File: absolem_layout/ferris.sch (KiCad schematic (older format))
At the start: 103 parts, among them IC1 NUF2221W1T2G, J1 USB C, K0_0 KEYSW, K0_1 KEYSW, K0_2 KEYSW, K0_3 KEYSW, K0_4 KEYSW, K0_5 KEYSW, K0_6 KEYSW, K0_7 KEYSW, K0_8 KEYSW, K0_9 KEYSW, K1_0 KEYSW, K1_1 KEYSW, K1_2 KEYSW, K1_3 KEYSW, K1_4 KEYSW, K1_5 KEYSW, K1_6 KEYSW, K1_7 KEYSW, K1_8 KEYSW, K1_9 KEYSW, K2_0 KEYSW, K2_1 KEYSW, K2_2 KEYSW, K2_3 KEYSW, K2_4 KEYSW, K2_5 KEYSW, K2_6 KEYSW, K2_7 KEYSW, K2_8 KEYSW, K2_9 KEYSW, K3_2 KEYSW, K3_3 KEYSW, K3_4 KEYSW, K3_5 KEYSW, K3_6 KEYSW, K3_7 KEYSW, SW1 SW_PUSH, SW2 SW_PUSH, U1 ATmega32U4-AU, U2 TLV70012_SOT23-5, U3 STM32F303CBTx, Y1 Crystal, Y2 8MHz

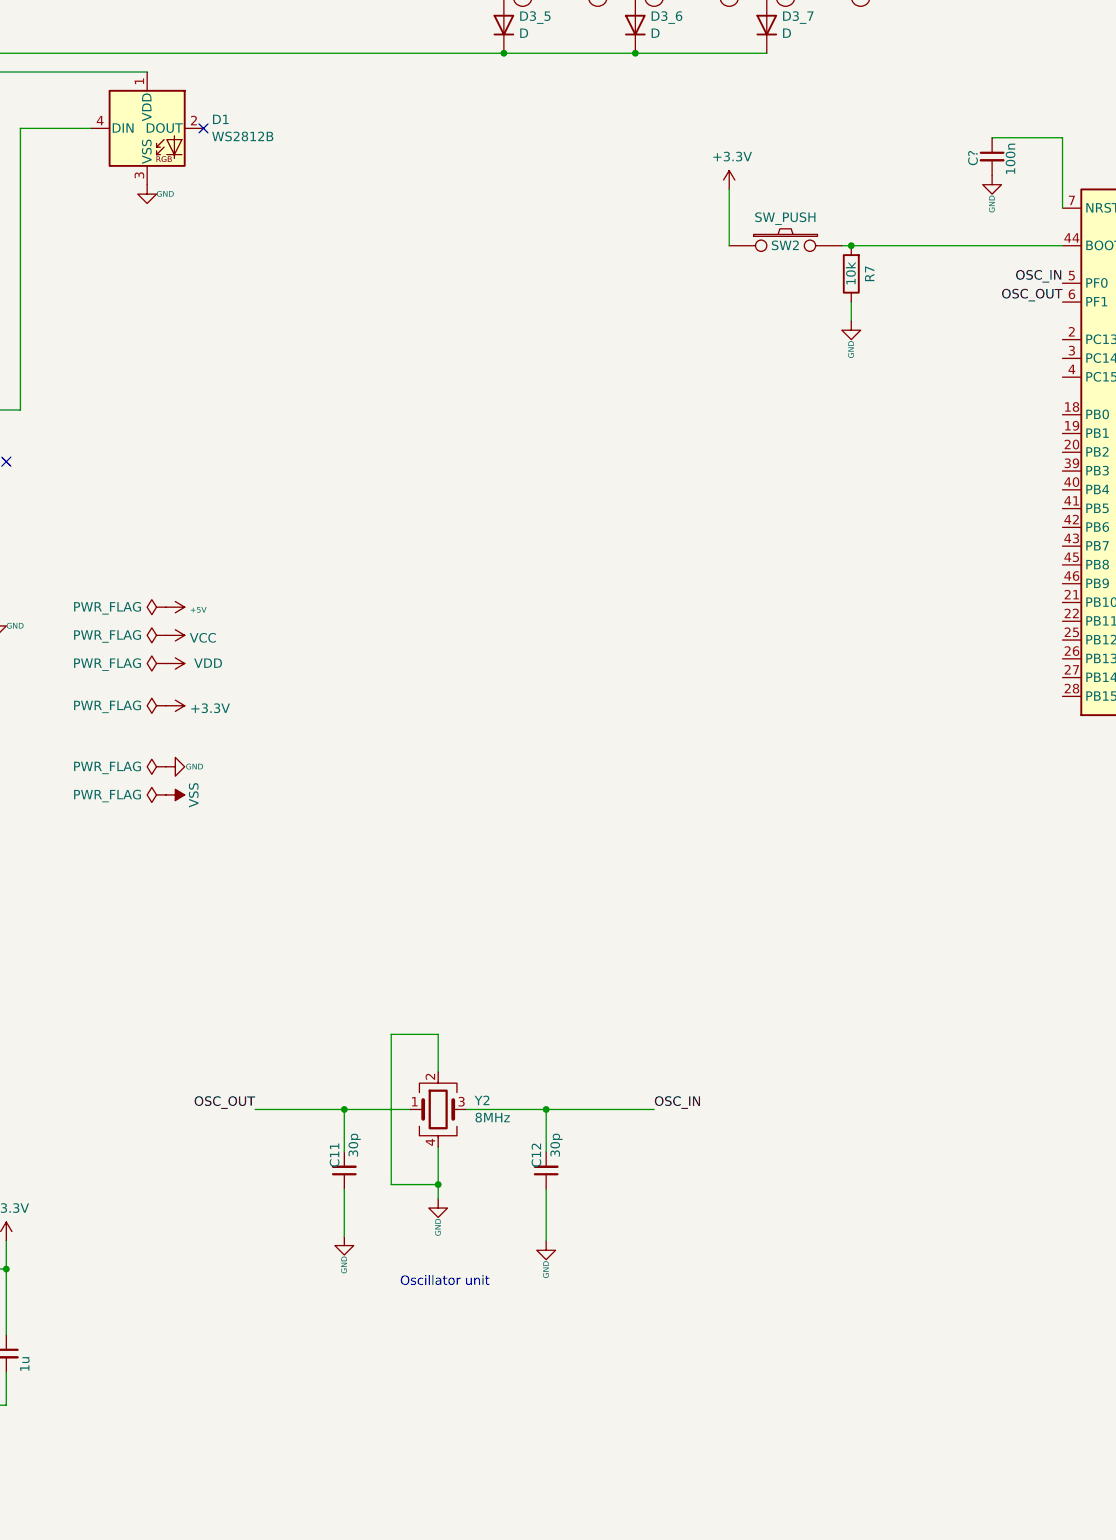
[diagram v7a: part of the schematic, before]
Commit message: More labelling
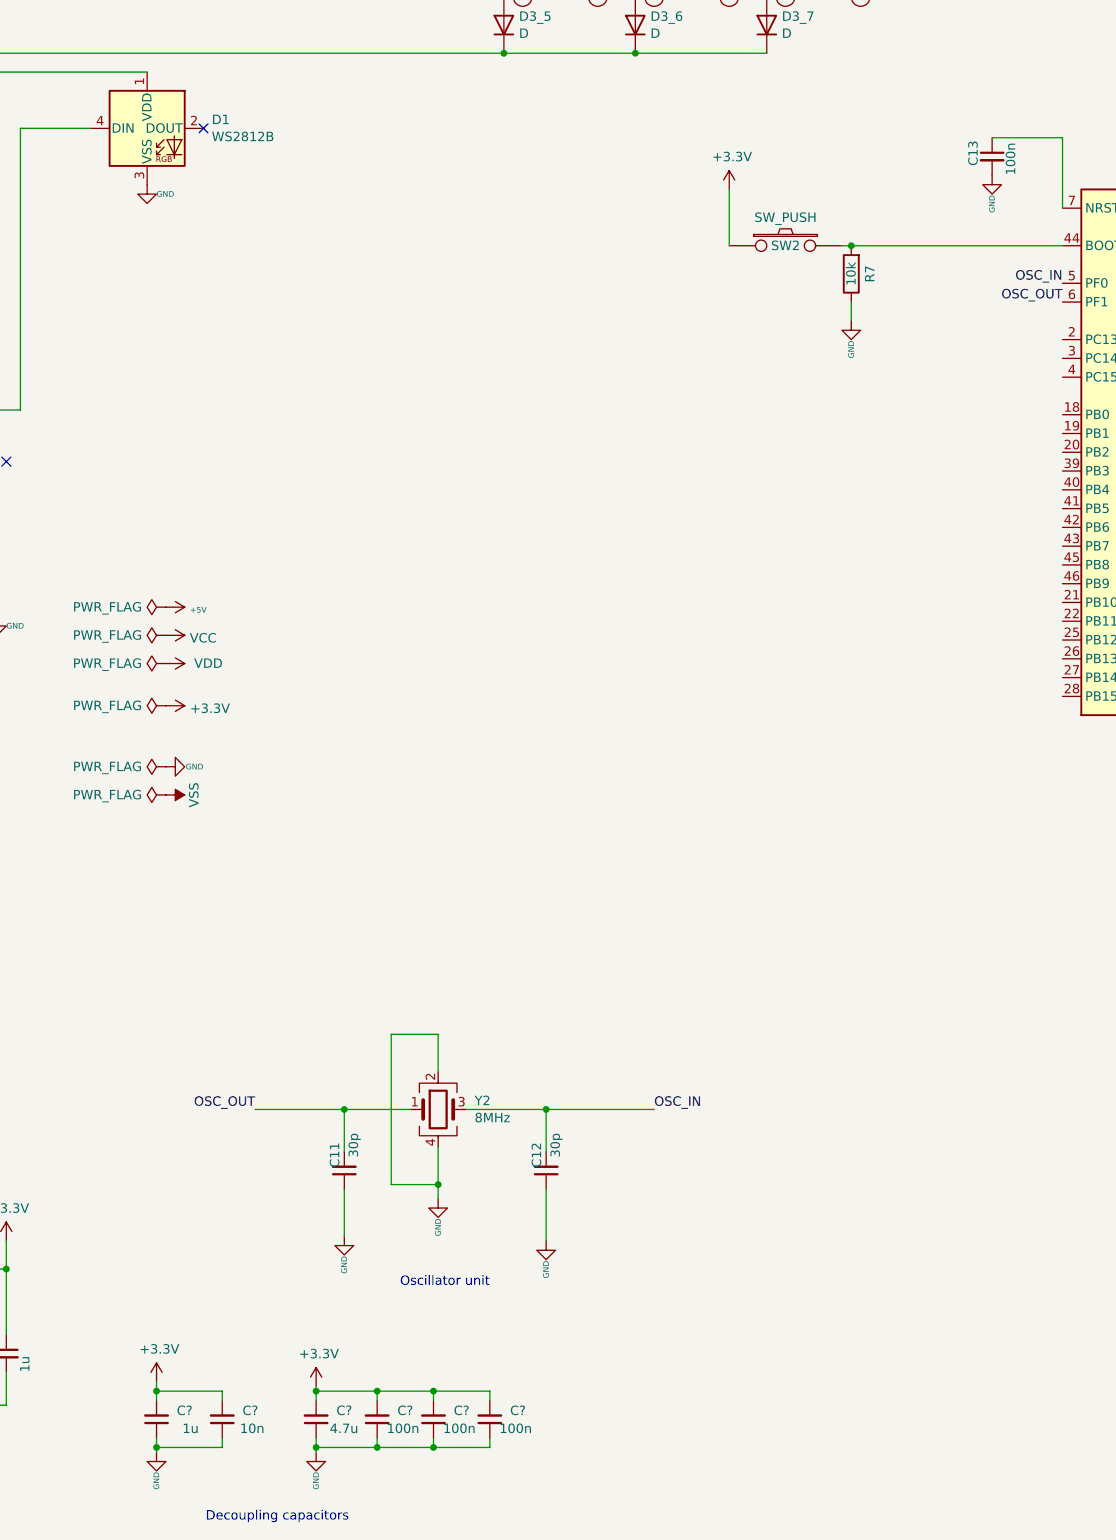
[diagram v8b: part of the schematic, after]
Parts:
- added C?: 1u, Capacitor_SMD:C_0805_2012Metric_Pad1.15x1.40mm_HandSolder, symbol ferris-rescue:C_Small-Device
- added C?: 10n, Capacitor_SMD:C_0805_2012Metric_Pad1.15x1.40mm_HandSolder, symbol ferris-rescue:C_Small-Device
- added C?: 4.7u, Capacitor_SMD:C_0805_2012Metric_Pad1.15x1.40mm_HandSolder, symbol ferris-rescue:C_Small-Device
- added C? (x3): 100n, Capacitor_SMD:C_0805_2012Metric_Pad1.15x1.40mm_HandSolder, symbol ferris-rescue:C_Small-Device
- gave numbers to parts that had none: 1
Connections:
- net +3V3: now also C?.2, C?.2, C?.2, C?.2, C?.2, C?.2
- net GND: now also C?.1, C?.1, C?.1, C?.1, C?.1, C?.1
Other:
- note added: "Decoupling capacitors"
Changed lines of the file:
@@
 	10125 3750 9750 3750
 $Comp
-L ferris-rescue:C_Small-Device C?
+L ferris-rescue:C_Small-Device C13
 U 1 1 5F35F244
 P 9750 3850
-F 0 "C?" V 9650 3800 50  0000 L CNN
+F 0 "C13" V 9650 3800 50  0000 L CNN
 F 1 "100n" V 9850 3750 50  0000 L CNN
 F 2 "Capacitor_SMD:C_0805_2012Metric_Pad1.15x1.40mm_HandSolder" H 9750 3850 50  0001 C CNN
@@
 $EndComp
 $Comp
-L ferris-rescue:GND-power #PWR?
+L ferris-rescue:GND-power #PWR0134
 U 1 1 5F397A3F
 P 9750 3950
-F 0 "#PWR?" H 9750 4000 20  0001 C CNN
+F 0 "#PWR0134" H 9750 4000 20  0001 C CNN
 F 1 "GND" V 9750 3750 30  0000 L CNN
 F 2 "" H 9750 3950 60  0000 C CNN
@@
 	1    0    0    -1
 $EndComp
+$Comp
+L ferris-rescue:+3.3V-power #PWR?
+U 1 1 5F491F96
+P 5300 10375
+F 0 "#PWR?" H 5300 10225 50  0001 C CNN
+F 1 "+3.3V" H 5315 10548 50  0000 C CNN
+F 2 "" H 5300 10375 50  0001 C CNN
+F 3 "" H 5300 10375 50  0001 C CNN
+	1    5300 10375
+	1    0    0    -1
+$EndComp
+$Comp
+L ferris-rescue:+3.3V-power #PWR?
+U 1 1 5F492655
+P 6150 10400
+F 0 "#PWR?" H 6150 10250 50  0001 C CNN
+F 1 "+3.3V" H 6165 10573 50  0000 C CNN
+F 2 "" H 6150 10400 50  0001 C CNN
+F 3 "" H 6150 10400 50  0001 C CNN
+	1    6150 10400
+	1    0    0    -1
+$EndComp
+$Comp
+L ferris-rescue:GND-power #PWR?
+U 1 1 5F4928A2
+P 5300 10750
+F 0 "#PWR?" H 5300 10800 20  0001 C CNN
+F 1 "GND" V 5300 10550 30  0000 L CNN
+F 2 "" H 5300 10750 60  0000 C CNN
+F 3 "" H 5300 10750 60  0000 C CNN
+	1    5300 10750
+	1    0    0    -1
+$EndComp
+$Comp
+L ferris-rescue:GND-power #PWR?
+U 1 1 5F492B9C
+P 6150 10750
+F 0 "#PWR?" H 6150 10800 20  0001 C CNN
+F 1 "GND" V 6150 10550 30  0000 L CNN
+F 2 "" H 6150 10750 60  0000 C CNN
+F 3 "" H 6150 10750 60  0000 C CNN
+	1    6150 10750
+	1    0    0    -1
+$EndComp
+$Comp
+L ferris-rescue:C_Small-Device C?
+U 1 1 5F493E8A
+P 5300 10575
+F 0 "C?" H 5150 10500 50  0000 C BNN
+F 1 "1u" H 5075 10625 50  0000 L CNN
+F 2 "Capacitor_SMD:C_0805_2012Metric_Pad1.15x1.40mm_HandSolder" H 5300 10575 50  0001 C CNN
+F 3 "~" H 5300 10575 50  0001 C CNN
+	1    5300 10575
+	-1   0    0    1
+$EndComp
+$Comp
+L ferris-rescue:C_Small-Device C?
+U 1 1 5F495876
+P 5650 10575
+F 0 "C?" H 5500 10500 50  0000 C BNN
+F 1 "10n" H 5425 10625 50  0000 L CNN
+F 2 "Capacitor_SMD:C_0805_2012Metric_Pad1.15x1.40mm_HandSolder" H 5650 10575 50  0001 C CNN
+F 3 "~" H 5650 10575 50  0001 C CNN
+	1    5650 10575
+	-1   0    0    1
+$EndComp
+$Comp
+L ferris-rescue:C_Small-Device C?
+U 1 1 5F495EE0
+P 6150 10575
+F 0 "C?" H 6000 10500 50  0000 C BNN
+F 1 "4.7u" H 5925 10625 50  0000 L CNN
+F 2 "Capacitor_SMD:C_0805_2012Metric_Pad1.15x1.40mm_HandSolder" H 6150 10575 50  0001 C CNN
+F 3 "~" H 6150 10575 50  0001 C CNN
+	1    6150 10575
+	-1   0    0    1
+$EndComp
+$Comp
+L ferris-rescue:C_Small-Device C?
+U 1 1 5F496832
+P 6475 10575
+F 0 "C?" H 6325 10500 50  0000 C BNN
+F 1 "100n" H 6250 10625 50  0000 L CNN
+F 2 "Capacitor_SMD:C_0805_2012Metric_Pad1.15x1.40mm_HandSolder" H 6475 10575 50  0001 C CNN
+F 3 "~" H 6475 10575 50  0001 C CNN
+	1    6475 10575
+	-1   0    0    1
+$EndComp
+$Comp
+L ferris-rescue:C_Small-Device C?
+U 1 1 5F496C31
+P 6775 10575
+F 0 "C?" H 6625 10500 50  0000 C BNN
+F 1 "100n" H 6550 10625 50  0000 L CNN
+F 2 "Capacitor_SMD:C_0805_2012Metric_Pad1.15x1.40mm_HandSolder" H 6775 10575 50  0001 C CNN
+F 3 "~" H 6775 10575 50  0001 C CNN
+	1    6775 10575
+	-1   0    0    1
+$EndComp
+$Comp
+L ferris-rescue:C_Small-Device C?
+U 1 1 5F496E51
+P 7075 10575
+F 0 "C?" H 6925 10500 50  0000 C BNN
+F 1 "100n" H 6850 10625 50  0000 L CNN
+F 2 "Capacitor_SMD:C_0805_2012Metric_Pad1.15x1.40mm_HandSolder" H 7075 10575 50  0001 C CNN
+F 3 "~" H 7075 10575 50  0001 C CNN
+	1    7075 10575
+	-1   0    0    1
+$EndComp
+Wire Wire Line
+	5300 10375 5300 10425
+Wire Wire Line
+	5300 10425 5650 10425
+Wire Wire Line
+	5650 10425 5650 10475
+Connection ~ 5300 10425
+Wire Wire Line
+	5300 10425 5300 10475
+Wire Wire Line
+	5300 10675 5300 10725
+Wire Wire Line
+	5650 10675 5650 10725
+Wire Wire Line
+	5650 10725 5300 10725
+Connection ~ 5300 10725
+Wire Wire Line
+	5300 10725 5300 10750
+Wire Wire Line
+	6150 10400 6150 10425
+Wire Wire Line
+	6150 10675 6150 10725
+Wire Wire Line
+	6150 10425 6475 10425
+Wire Wire Line
+	7075 10425 7075 10475
+Connection ~ 6150 10425
+Wire Wire Line
+	6150 10425 6150 10475
+Wire Wire Line
+	7075 10675 7075 10725
+Wire Wire Line
+	7075 10725 6775 10725
+Connection ~ 6150 10725
+Wire Wire Line
+	6150 10725 6150 10750
+Wire Wire Line
+	6475 10475 6475 10425
+Connection ~ 6475 10425
+Wire Wire Line
+	6475 10425 6775 10425
+Wire Wire Line
+	6775 10475 6775 10425
+Connection ~ 6775 10425
+Wire Wire Line
+	6775 10425 7075 10425
+Wire Wire Line
+	6475 10675 6475 10725
+Connection ~ 6475 10725
+Wire Wire Line
+	6475 10725 6150 10725
+Wire Wire Line
+	6775 10675 6775 10725
+Connection ~ 6775 10725
+Wire Wire Line
+	6775 10725 6475 10725
+Text Notes 6325 11125 2    50   ~ 0
+Decoupling capacitors
 $EndSCHEMATC
